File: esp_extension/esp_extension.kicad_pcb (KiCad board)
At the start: 4 copper layers, 70 x 60.6 mm, 66 parts, among them J1 MOTOR1, J10 MPU6050, J2 MOTOR2, J3 MOTOR3, J4 MOTOR4, J5 ESP32-S3-LeftHeader, J6 BATTERY, J7 ESP32-S3-RightHeader, J8 I2C, J9 GPIO, Q1 AO3400A, Q2 AO3400A, Q3 AO3400A, Q4 AO3400A, SW1 SW_SPDT, U2 TPS63802DLAR, U3 MS5611-01BA

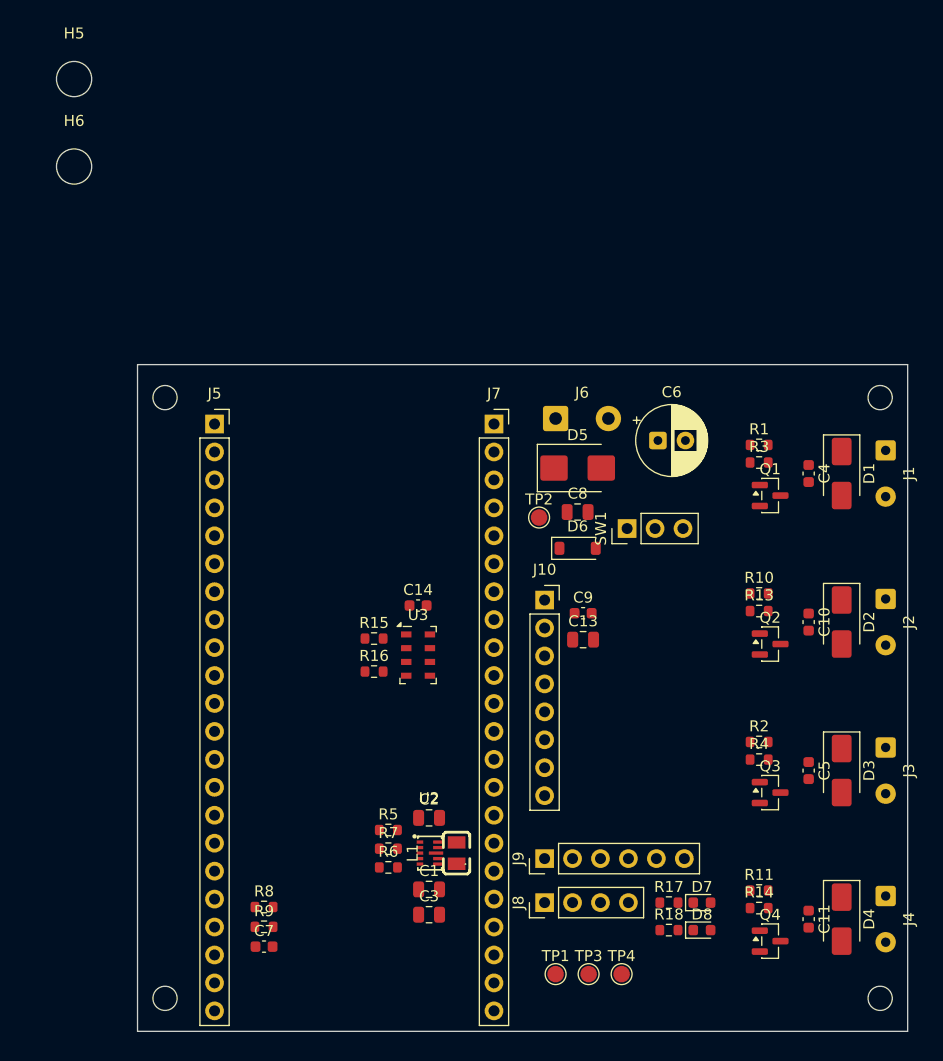
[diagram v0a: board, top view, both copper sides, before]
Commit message: Moved the motors to the left side as well
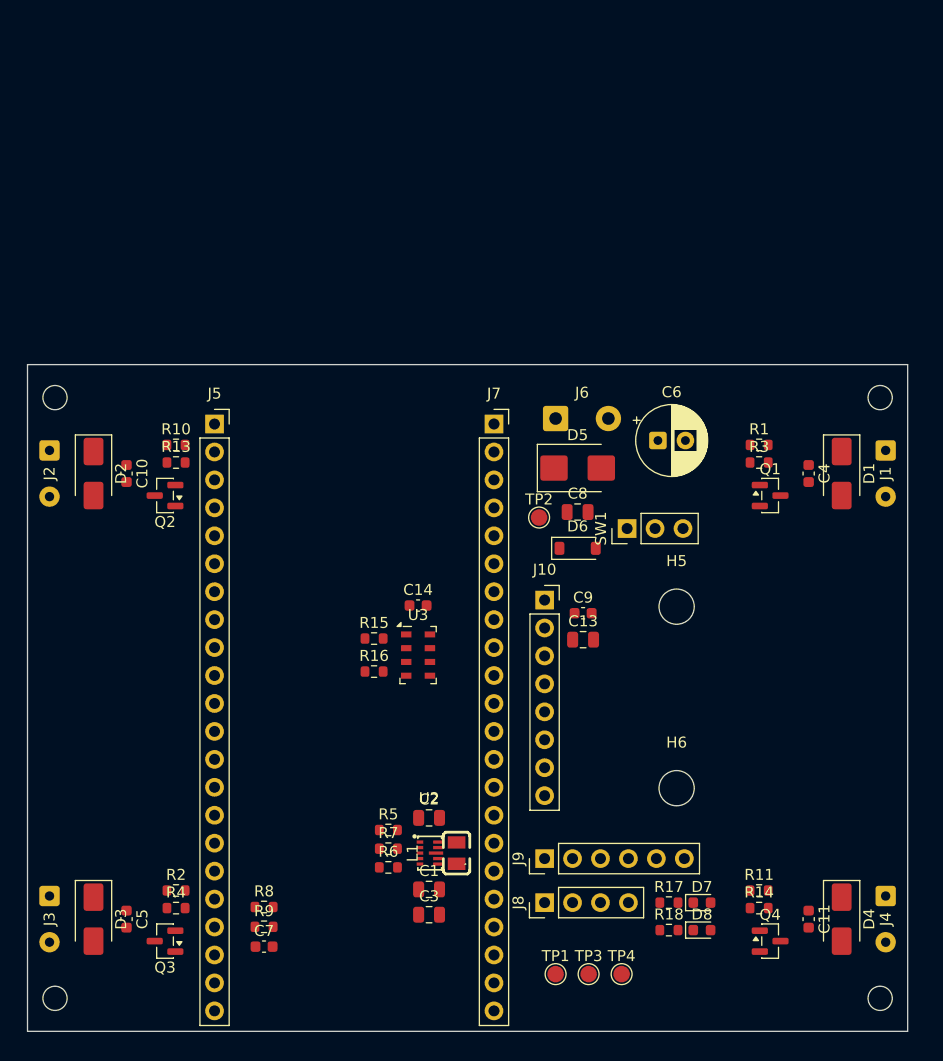
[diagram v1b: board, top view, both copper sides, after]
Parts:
- moved H6 78.7 mm to (142.0, 133.1)
- moved J2 77.2 mm to (85.0, 102.4)
- moved J3 77.2 mm to (85.0, 142.9)
- moved H5 72.8 mm to (142.0, 116.6)
- moved D2 69.3 mm to (89.0, 104.5)
- moved D3 69.3 mm to (89.0, 145.0)
- moved C10 63.5 mm to (92.0, 104.5)
- moved C5 63.5 mm to (92.0, 145.0)
- moved Q2 56.6 mm to (95.5, 106.5), turned to 180 degrees
- moved Q3 56.6 mm to (95.5, 147.0), turned to 180 degrees
- moved R10 54.7 mm to (96.5, 101.9)
- moved R13 54.7 mm to (96.5, 103.5)
- moved R2 54.7 mm to (96.5, 142.4)
- moved R4 54.7 mm to (96.5, 144.0)
- moved H1 10.0 mm to (85.5, 97.6)
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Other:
- board size 70 x 60.6 mm -> 80 x 60.6 mm

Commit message: Board ready for tracing
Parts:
- moved D7 60.5 mm to (88.5, 120.0)
- moved D8 60.0 mm to (88.5, 124.0)
- moved R17 54.6 mm to (92.0, 120.0)
- moved R18 54.0 mm to (92.0, 124.0)
- moved SW1 24.5 mm to (158.0, 123.0), turned to 0 degrees
- moved R13 10.7 mm to (95.5, 114.2)
- moved R10 10.7 mm to (95.5, 112.6)
- moved R3 10.7 mm to (150.3, 114.2)
- moved R1 10.7 mm to (150.3, 112.6)
- moved R4 8.76 mm to (95.5, 135.3)
- moved R14 8.74 mm to (150.3, 135.3)
- moved C8 8.28 mm to (140.5, 104.5)
- moved Q3 7.03 mm to (94.8, 140.0)
- moved Q4 7.03 mm to (151.2, 140.0)
- moved R2 5.59 mm to (95.5, 136.9)
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
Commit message: Voltage regulator routed
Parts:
- moved C2 0.55 mm to (118.7, 136.3), turned to 180 degrees
- turned C1 to 180 degrees
- turned C3 to 180 degrees
- turned R5 to 180 degrees
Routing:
- net +3V3: track 0.00 -> 22.0 mm
- net GND: track 0.00 -> 10.9 mm, vias 0 -> 6
- net Net-(U2-FB): track 0.00 -> 3.74 mm
- net Net-(U2-L2): track 0.00 -> 2.55 mm
- net Net-(U2-L1): track 0.00 -> 2.55 mm
- net Net-(SW1-B): track 0.00 -> 2.45 mm
- net VIN_3V3: track 0.00 -> 1.67 mm
- added copper zone on In2.Cu, net +BATT
- added copper zone on In1.Cu, net GND

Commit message: Autorouted and checked the entire board
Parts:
- moved J3 4.20 mm to (85.0, 147.1), turned to 90 degrees
- moved J4 4.20 mm to (161.0, 147.1), turned to 90 degrees
- turned C11 to 90 degrees
- turned C5 to 90 degrees
- turned D3 to 90 degrees
- turned D4 to 90 degrees
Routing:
- net +3V3: track 22.0 -> 142.7 mm
- net VIN_3V3: track 1.67 -> 96.0 mm, vias 0 -> 1
- net +BATT: track 0.00 -> 83.6 mm, vias 0 -> 2
- net MOTOR1_PWM: track 0.00 -> 59.3 mm, vias 0 -> 1
- net BARO_SCL: track 0.00 -> 56.9 mm, vias 0 -> 2
- net MOTOR2_PWM: track 0.00 -> 55.9 mm, vias 0 -> 1
- net Net-(SW1-B): track 2.45 -> 53.3 mm, vias 0 -> 1
- net BARO_SDA: track 0.00 -> 44.7 mm, vias 0 -> 2
- net MOTOR3_PWM: track 0.00 -> 34.3 mm, vias 0 -> 1
- net IMU_INT: track 0.00 -> 32.3 mm
- net GND: track 10.9 -> 42.2 mm, vias 6 -> 31
- net LED_INDICATOR: track 0.00 -> 29.1 mm
- net MOTOR4_PWM: track 0.00 -> 28.2 mm, vias 0 -> 1
- net GPIO_18: track 0.00 -> 23.0 mm
- net GPIO_17: track 0.00 -> 19.4 mm
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- added copper zone on B.Cu, net GND
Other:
- board text added: "+"
- board text added: "−"
